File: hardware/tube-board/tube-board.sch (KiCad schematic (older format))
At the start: 18 parts, among them J1 CONN_01X10, J2 CONN_01X10, U1 HV5522PG, U2 HV5522PG

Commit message: Switched to an 0603 capacitor on tube board
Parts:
- C1, C2: footprint Capacitors_SMD:C_0805 -> Capacitors_SMD:C_0603; Part 311-1140-1-ND -> 311-1344-1-ND
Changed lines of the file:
@@
 F 0 "C1" H 2925 4100 50  0000 L CNN
 F 1 "0.1u" H 2925 3900 50  0000 L CNN
-F 2 "Capacitors_SMD:C_0805" H 2938 3850 50  0001 C CNN
+F 2 "Capacitors_SMD:C_0603" H 2938 3850 50  0001 C CNN
 F 3 "" H 2900 4000 50  0001 C CNN
 F 4 "DigiKey" H 2900 4000 60  0001 C CNN "Source"
-F 5 "311-1140-1-ND" H 2900 4000 60  0001 C CNN "Part"
+F 5 "311-1344-1-ND" H 2900 4000 60  0001 C CNN "Part"
 	1    2900 4000
 	1    0    0    -1
@@
 F 0 "C2" H 8025 4150 50  0000 L CNN
 F 1 "0.1u" H 8025 3950 50  0000 L CNN
-F 2 "Capacitors_SMD:C_0805" H 8038 3900 50  0001 C CNN
+F 2 "Capacitors_SMD:C_0603" H 8038 3900 50  0001 C CNN
 F 3 "" H 8000 4050 50  0001 C CNN
 F 4 "DigiKey" H 8000 4050 60  0001 C CNN "Source"
-F 5 "311-1140-1-ND" H 8000 4050 60  0001 C CNN "Part"
+F 5 "311-1344-1-ND" H 8000 4050 60  0001 C CNN "Part"
 	1    8000 4050
 	1    0    0    -1

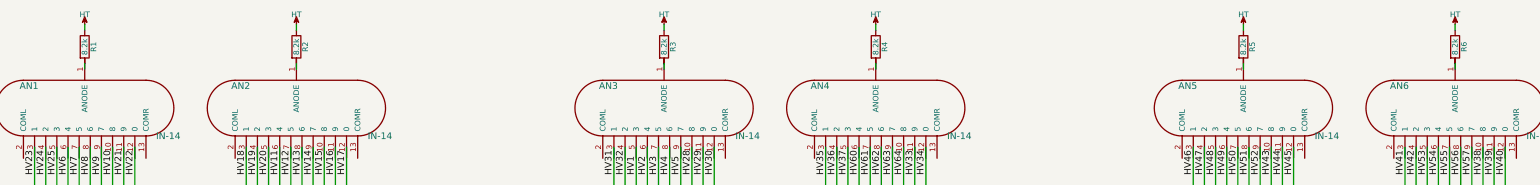
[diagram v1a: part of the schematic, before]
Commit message: Updated current limit resistors for nixie tubes
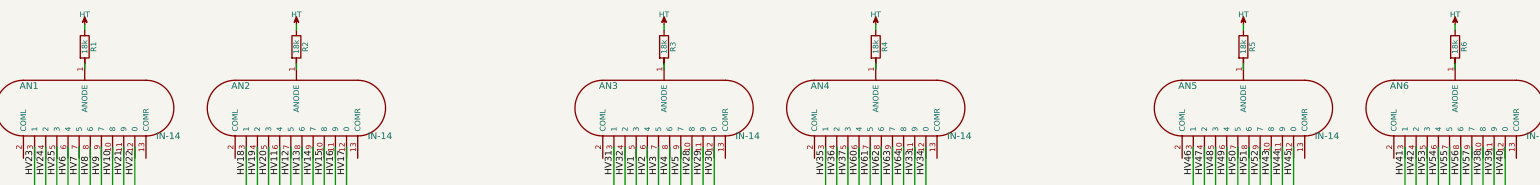
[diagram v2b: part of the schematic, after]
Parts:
- R1, R2, R3, R4, R5, R6: value 8.2k -> 18k; Part 311-8.20KFRCT-ND -> (none)
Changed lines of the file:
@@
 P 2300 1400
 F 0 "R1" V 2380 1400 50  0000 C CNN
-F 1 "8.2k" V 2300 1400 50  0000 C CNN
+F 1 "18k" V 2300 1400 50  0000 C CNN
 F 2 "Resistors_SMD:R_1206" V 2230 1400 50  0001 C CNN
 F 3 "" H 2300 1400 50  0001 C CNN
 F 4 "DigiKey" H 2300 1400 60  0001 C CNN "Source"
-F 5 "311-8.20KFRCT-ND" H 2300 1400 60  0001 C CNN "Part"
 	1    2300 1400
 	1    0    0    -1
@@
 P 4200 1400
 F 0 "R2" V 4280 1400 50  0000 C CNN
-F 1 "8.2k" V 4200 1400 50  0000 C CNN
+F 1 "18k" V 4200 1400 50  0000 C CNN
 F 2 "Resistors_SMD:R_1206" V 4130 1400 50  0001 C CNN
 F 3 "" H 4200 1400 50  0001 C CNN
 F 4 "DigiKey" H 4200 1400 60  0001 C CNN "Source"
-F 5 "311-8.20KFRCT-ND" H 4200 1400 60  0001 C CNN "Part"
 	1    4200 1400
 	1    0    0    -1
@@
 P 7500 1400
 F 0 "R3" V 7580 1400 50  0000 C CNN
-F 1 "8.2k" V 7500 1400 50  0000 C CNN
+F 1 "18k" V 7500 1400 50  0000 C CNN
 F 2 "Resistors_SMD:R_1206" V 7430 1400 50  0001 C CNN
 F 3 "" H 7500 1400 50  0001 C CNN
 F 4 "DigiKey" H 7500 1400 60  0001 C CNN "Source"
-F 5 "311-8.20KFRCT-ND" H 7500 1400 60  0001 C CNN "Part"
 	1    7500 1400
 	1    0    0    -1
@@
 P 9400 1400
 F 0 "R4" V 9480 1400 50  0000 C CNN
-F 1 "8.2k" V 9400 1400 50  0000 C CNN
+F 1 "18k" V 9400 1400 50  0000 C CNN
 F 2 "Resistors_SMD:R_1206" V 9330 1400 50  0001 C CNN
 F 3 "" H 9400 1400 50  0001 C CNN
 F 4 "DigiKey" H 9400 1400 60  0001 C CNN "Source"
-F 5 "311-8.20KFRCT-ND" H 9400 1400 60  0001 C CNN "Part"
 	1    9400 1400
 	1    0    0    -1
@@
 P 12700 1400
 F 0 "R5" V 12780 1400 50  0000 C CNN
-F 1 "8.2k" V 12700 1400 50  0000 C CNN
+F 1 "18k" V 12700 1400 50  0000 C CNN
 F 2 "Resistors_SMD:R_1206" V 12630 1400 50  0001 C CNN
 F 3 "" H 12700 1400 50  0001 C CNN
 F 4 "DigiKey" H 12700 1400 60  0001 C CNN "Source"
-F 5 "311-8.20KFRCT-ND" H 12700 1400 60  0001 C CNN "Part"
 	1    12700 1400
 	1    0    0    -1
@@
 P 14600 1400
 F 0 "R6" V 14680 1400 50  0000 C CNN
-F 1 "8.2k" V 14600 1400 50  0000 C CNN
+F 1 "18k" V 14600 1400 50  0000 C CNN
 F 2 "Resistors_SMD:R_1206" V 14530 1400 50  0001 C CNN
 F 3 "" H 14600 1400 50  0001 C CNN
 F 4 "DigiKey" H 14600 1400 60  0001 C CNN "Source"
-F 5 "311-8.20KFRCT-ND" H 14600 1400 60  0001 C CNN "Part"
 	1    14600 1400
 	1    0    0    -1
